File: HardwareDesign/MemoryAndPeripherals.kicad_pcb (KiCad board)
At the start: 2 copper layers, 150 x 90 mm, 29 parts, among them J001 Conn_02x40_Odd_Even, J303 Conn_01x05, J304 Conn_01x05, J305 Conn_01x09, J306 Conn_01x09, U200 28C256, U201 62256 (32 KB SRAM), U301 82C55A, U302 82C54, U303 MC6850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

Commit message: add URL, minor silkscreen tweak
Is ready to fab?
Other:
- board text added: "https://github.com/daveho/DIY8bit"

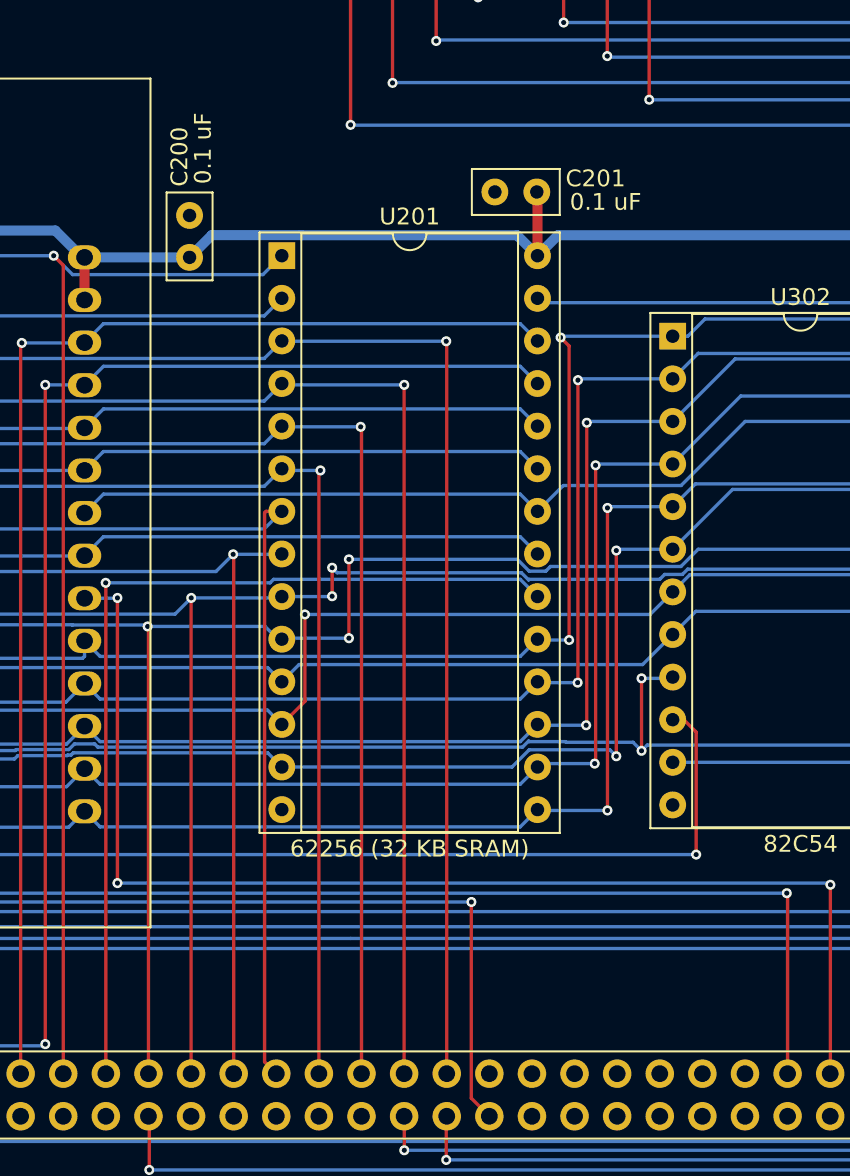
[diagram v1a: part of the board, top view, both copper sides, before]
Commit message: support jumper to select A15 or ~RAMEN~
This provides some future-proofing to use the board with
CPU/glue logic modules that have a different memory map.
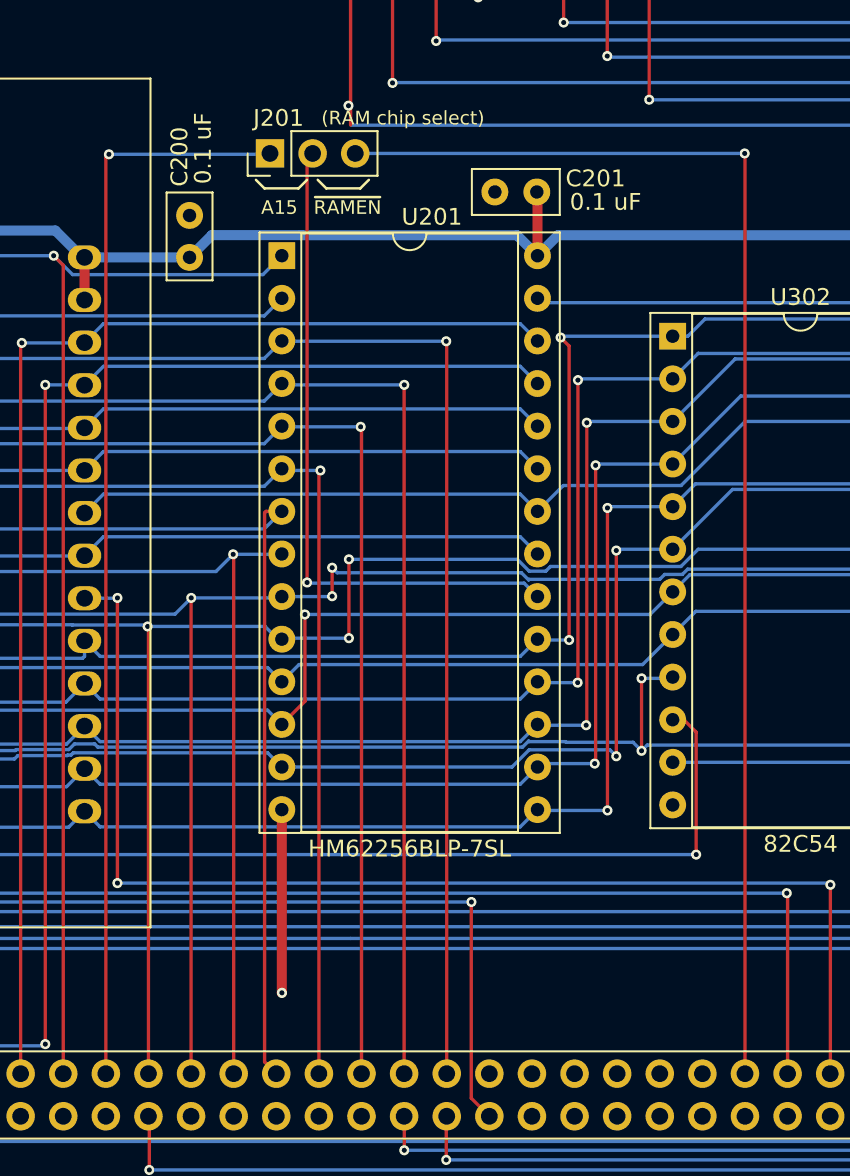
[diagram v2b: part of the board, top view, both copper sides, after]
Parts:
- added J201: Conn_01x03, Connector_PinHeader_2.54mm:PinHeader_1x03_P2.54mm_Vertical, F.Cu at (75.9, 25.6)
- U201: value 62256 (32 KB SRAM) -> HM62256BLP-7SL
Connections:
- J001 pad 64: Net-(J001-Pad64) -> /~RAMEN~
- U201 pad 20: /A15 -> Net-(J201-Pad2)
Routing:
- net /~RAMEN~: track 0.00 -> 78.1 mm, vias 0 -> 1
- net Net-(J201-Pad2): track 0.00 -> 39.8 mm, vias 0 -> 1
- net GND: track 0.76 -> 11.7 mm, vias 0 -> 1
- net /A15: track 55.5 -> 64.5 mm
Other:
- board text added: "(RAM chip select)"
- board text added: "A15"
- board text added: "~RAMEN~"

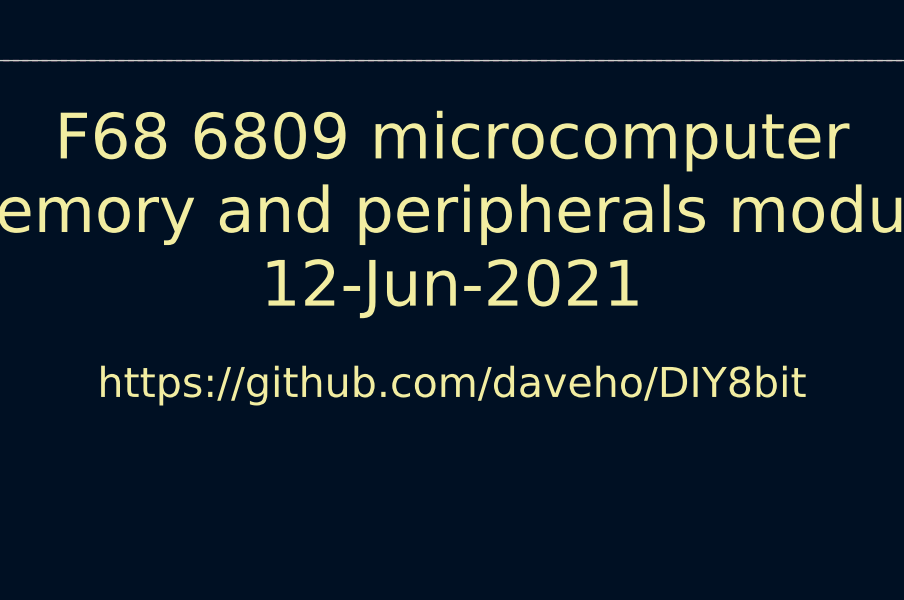
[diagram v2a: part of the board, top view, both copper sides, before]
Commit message: updated the date
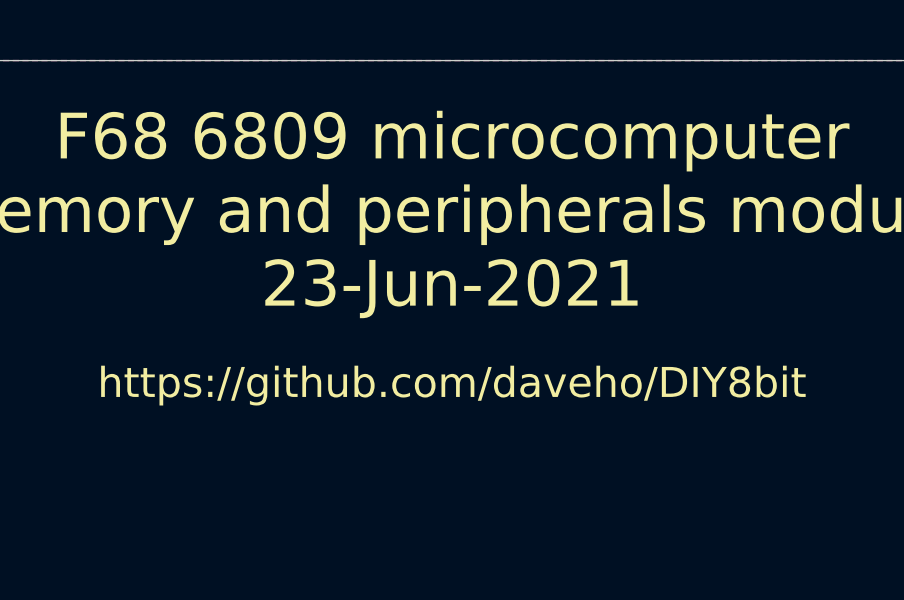
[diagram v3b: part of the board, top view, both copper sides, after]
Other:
- board text added: "F68 6809 microcomputer Memory and peripherals module 23-Jun-2021"
- board text removed: "F68 6809 microcomputer Memory and peripherals module 12-Jun-2021"
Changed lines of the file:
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@@
     (effects (font (size 1 1) (thickness 0.25)))
   )
-  (gr_text "F68 6809 microcomputer\nMemory and peripherals module\n12-Jun-2021" (at 60.72 5.01) (layer F.SilkS)
+  (gr_text "F68 6809 microcomputer\nMemory and peripherals module\n23-Jun-2021" (at 60.72 5.01) (layer F.SilkS)
     (effects (font (size 1.524 1.524) (thickness 0.3048)))
   )
